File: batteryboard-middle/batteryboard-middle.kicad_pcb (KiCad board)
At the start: 2 copper layers, 46.8 x 46.8 mm, 7 parts, among them J1 Conn 02x10 1.27mm, J2 Conn_01x02, J3 Conn_01x02

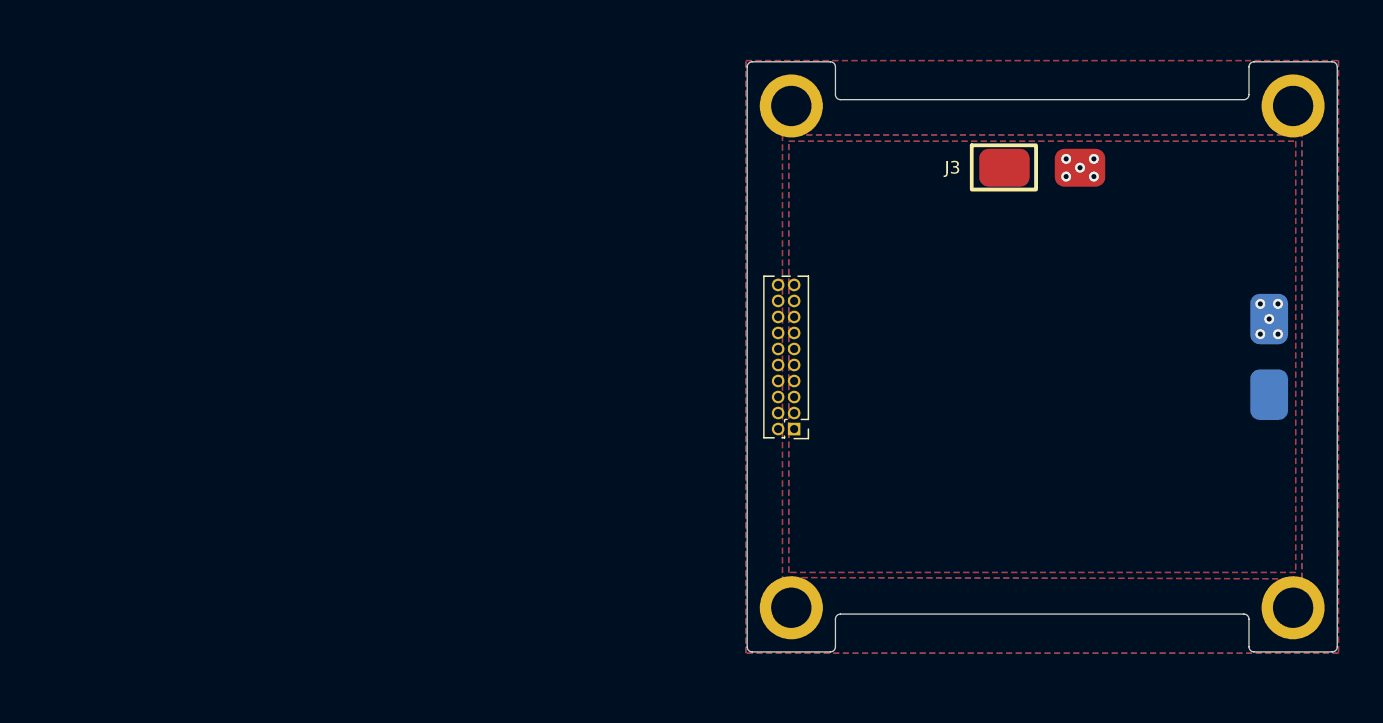
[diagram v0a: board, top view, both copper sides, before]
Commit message: Added proper connectors and added traces
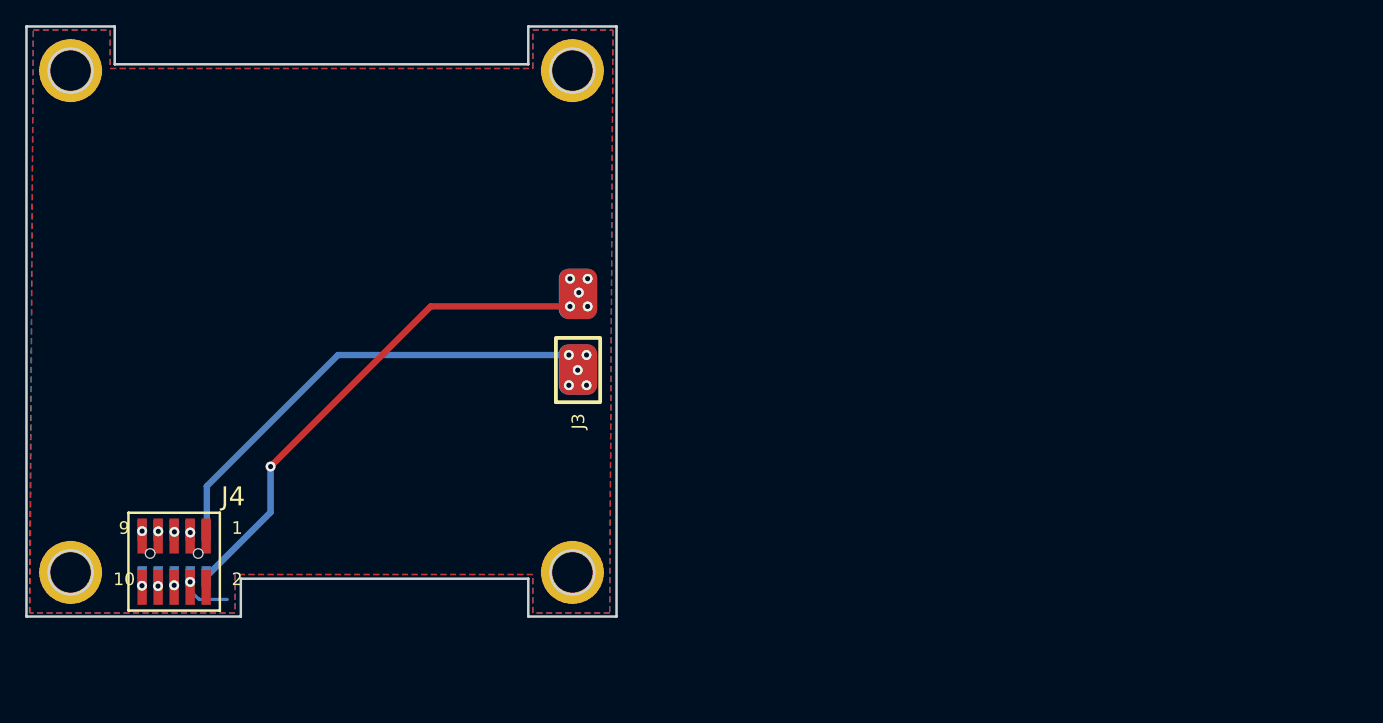
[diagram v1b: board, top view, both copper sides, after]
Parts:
- added J4: Conn_02x05_Odd_Even, batteryboard:SAMTEC-FTS-105-01-X-DV, F.Cu at (76.5, 114.0)
- J1: value Conn 02x10 1.27mm -> Conn_02x05_Odd_Even; footprint Connector_PinHeader_1.27mm:PinHeader_2x10_P1.27mm_Vertical -> batteryboard:SAMTEC_FLE-105-01-G-DV-A; moved to B.Cu
- moved H1 57.2 mm to (68.2, 75.1)
- moved H4 57.2 mm to (68.2, 114.9)
- moved H2 57.2 mm to (108.0, 75.1)
- moved H3 57.2 mm to (108.0, 114.9)
- moved J2 54.9 mm to (108.5, 95.8), turned to 90 degrees
- moved J1 50.2 mm to (76.5, 113.4)
- moved J3 39.0 mm to (108.5, 95.8), turned to 90 degrees
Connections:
- J1 pad 10: unconnected-(J1-Pad10) -> VBUS
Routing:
- net BATT_N_SW: track 0.00 -> 39.9 mm, vias 5 -> 6
- net BATT_P_SW: track 0.00 -> 36.5 mm
- net GND: track 0.00 -> 4.33 mm, vias 0 -> 1
- net VBUS: vias 0 -> 1
- net SDA3: vias 0 -> 1
- net SCL3: vias 0 -> 1
- net COIL_P: vias 0 -> 1
- net COIL_N: vias 0 -> 1
- net BATT_P: vias 0 -> 1
- net +3V3: vias 0 -> 1
- removed copper zone on B.Cu, net BATT_N_SW
- removed copper zone on F.Cu, net BATT_P_SW
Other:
- outline, holes or cut-outs redrawn

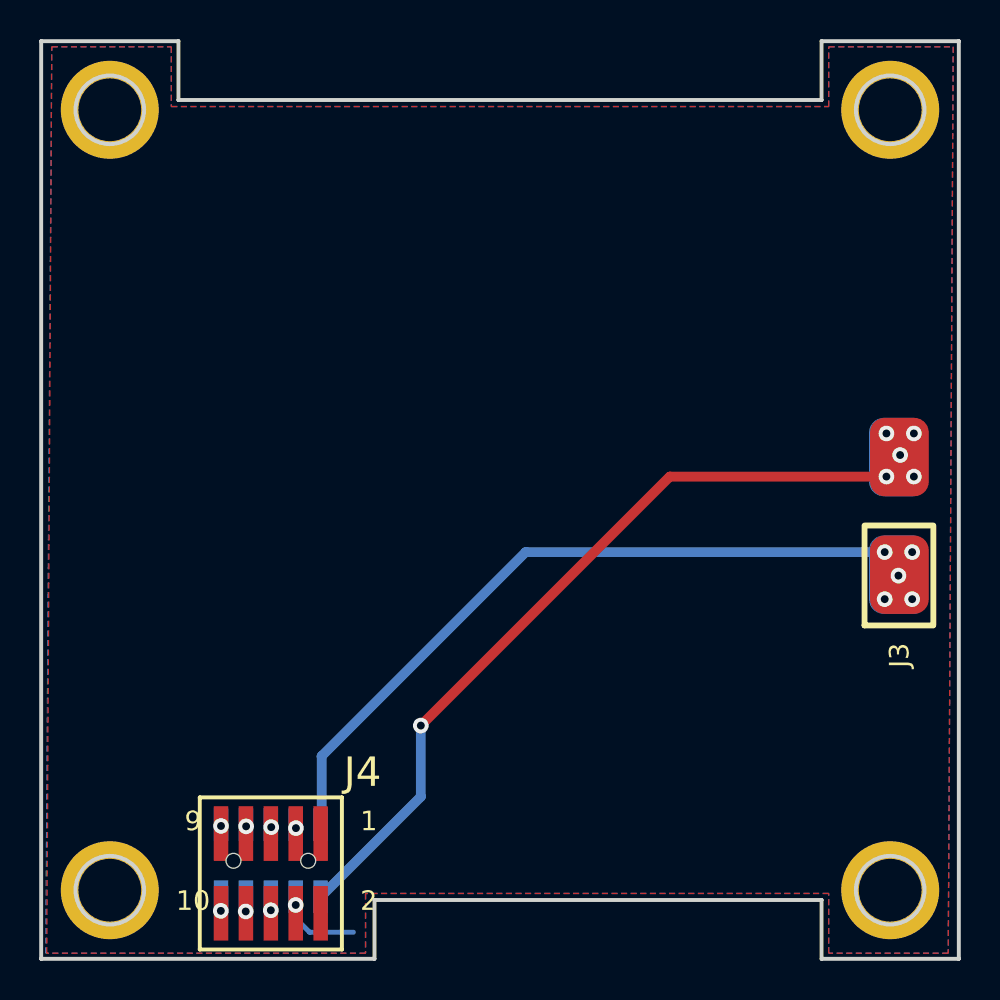
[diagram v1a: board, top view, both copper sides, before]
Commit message: Fixed design errors (some issues remain in middle) and fixed trace widths
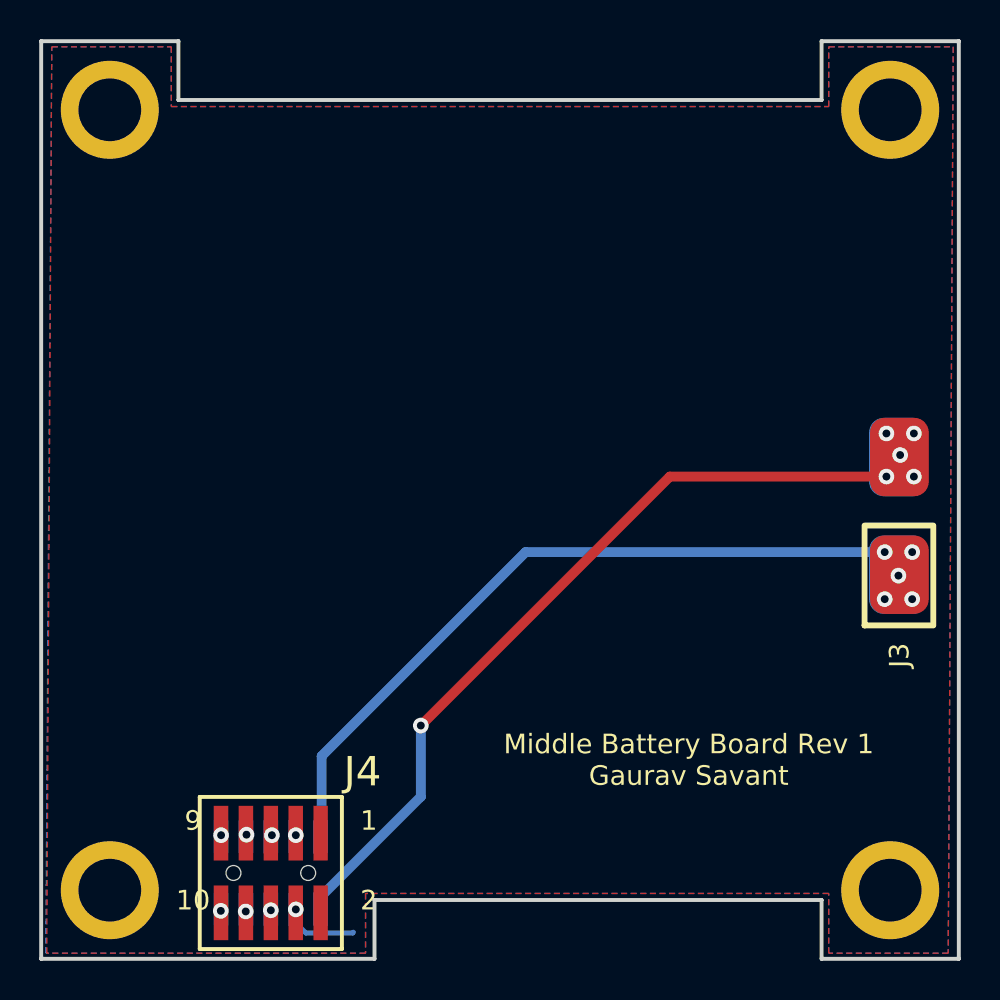
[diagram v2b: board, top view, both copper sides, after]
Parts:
- moved J1 0.62 mm to (76.5, 114.0)
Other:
- outline, holes or cut-outs redrawn
- board text added: "Middle Battery Board Rev 1 Gaurav Savant"
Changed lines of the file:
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@@
   )
   (footprint "batteryboard:SAMTEC-FTS-105-01-X-DV" (layer "F.Cu")
-    (at 76.45 114.042 180)
+    (at 76.45 114.018 180)
     (descr "translated Allegro footprint")
     (property "Sheetfile" "batteryboard-middle.kicad_sch")
@@
   )
   (footprint "batteryboard:SAMTEC_FLE-105-01-G-DV-A" (layer "B.Cu")
-    (at 76.45 113.396 180)
+    (at 76.45 114.018 180)
     (property "Sheetfile" "batteryboard-middle.kicad_sch")
     (property "Sheetname" "")
@@
     (fp_line (start -3.175 1.665) (end 3.175 1.665) (layer "B.Fab") (width 0.1))
     (fp_circle (center -2.85 3.44) (end -2.75 3.44) (layer "B.Fab") (width 0.2) (fill none))
-    (pad "" np_thru_hole circle (at 1.905 0 180) (size 0.76 0.76) (drill 0.76) (layers *.Cu *.Mask))
+    (pad "" np_thru_hole circle (at 1.904988 -0.000009 180) (size 0.76 0.76) (drill 0.76) (layers F&B.Cu *.Mask))
     (pad "" np_thru_hole circle (at -1.905 0 180) (size 0.76 0.76) (drill 0.76) (layers *.Cu *.Mask))
     (pad "01" smd rect (at -2.54 1.8425 180) (size 0.74 1.675) (layers "B.Cu" "B.Paste" "B.Mask")
@@
     )
   )
-  (gr_circle (center 68.238 75.096) (end 69.988 75.096) (layer "Edge.Cuts") (width 0.2) (fill none))
-  (gr_circle (center 108.038 114.896) (end 109.788 114.896) (layer "Edge.Cuts") (width 0.2) (fill none))
-  (gr_circle (center 68.238 114.896) (end 69.988 114.896) (layer "Edge.Cuts") (width 0.2) (fill none))
   (gr_line (start 81.738 115.396) (end 81.738 118.396) (layer "Edge.Cuts") (width 0.2))
   (gr_line (start 104.538 118.396) (end 111.538 118.396) (layer "Edge.Cuts") (width 0.2))
   (gr_line (start 104.538 74.596) (end 71.738 74.596) (layer "Edge.Cuts") (width 0.2))
-  (gr_circle (center 108.038 75.096) (end 109.788 75.096) (layer "Edge.Cuts") (width 0.2) (fill none))
   (gr_line (start 104.538 71.596) (end 104.538 74.596) (layer "Edge.Cuts") (width 0.2))
   (gr_line (start 64.738 71.596) (end 64.738 118.396) (layer "Edge.Cuts") (width 0.2))
@@
   (gr_line (start 111.538 71.596) (end 104.538 71.596) (layer "Edge.Cuts") (width 0.2))
   (gr_line (start 111.538 71.596) (end 111.538 118.396) (layer "Edge.Cuts") (width 0.2))
+  (gr_text "Middle Battery Board Rev 1\nGaurav Savant\n" (at 97.7646 108.2548) (layer "F.SilkS")
+    (effects (font (size 1 1) (thickness 0.15)))
+  )
   (via (at 109.158 97.6532) (size 0.8) (drill 0.4) (layers "F.Cu" "B.Cu") (net 1))
   (via (at 107.758 100.0532) (size 0.8) (drill 0.4) (layers "F.Cu" "B.Cu") (net 1))
@@
   (segment (start 78.99 115.2385) (end 84.1 110.1285) (width 0.5) (layer "B.Cu") (net 2))
   (segment (start 84.1 110.1285) (end 84.1 106.5) (width 0.5) (layer "B.Cu") (net 2))
-  (via (at 77.72 115.65) (size 0.8) (drill 0.4) (layers "F.Cu" "B.Cu") (net 3))
-  (segment (start 78.43 117.04) (end 80.66 117.04) (width 0.254) (layer "B.Cu") (net 3))
-  (segment (start 77.72 115.2385) (end 77.72 115.65) (width 0.254) (layer "B.Cu") (net 3))
-  (segment (start 77.72 115.65) (end 77.72 116.33) (width 0.254) (layer "B.Cu") (net 3))
-  (segment (start 77.72 116.33) (end 78.43 117.04) (width 0.254) (layer "B.Cu") (net 3))
-  (via (at 77.73 111.73) (size 0.8) (drill 0.4) (layers "F.Cu" "B.Cu") (net 4))
-  (via (at 76.47 111.68) (size 0.8) (drill 0.4) (layers "F.Cu" "B.Cu") (net 5))
+  (via (at 77.724 115.8748) (size 0.8) (drill 0.4) (layers "F.Cu" "B.Cu") (net 3))
+  (segment (start 77.724 116.563022) (end 78.239489 117.078511) (width 0.254) (layer "B.Cu") (net 3))
+  (segment (start 80.621489 117.078511) (end 80.66 117.04) (width 0.254) (layer "B.Cu") (net 3))
+  (segment (start 77.72 115.2385) (end 77.72 115.8708) (width 0.254) (layer "B.Cu") (net 3))
+  (segment (start 77.724 115.8748) (end 77.724 116.563022) (width 0.254) (layer "B.Cu") (net 3))
+  (segment (start 77.72 115.8708) (end 77.724 115.8748) (width 0.254) (layer "B.Cu") (net 3))
+  (segment (start 78.239489 117.078511) (end 80.621489 117.078511) (width 0.254) (layer "B.Cu") (net 3))
+  (via (at 77.724 112.0902) (size 0.8) (drill 0.4) (layers "F.Cu" "B.Cu") (net 4))
+  (via (at 76.5048 112.0902) (size 0.8) (drill 0.4) (layers "F.Cu" "B.Cu") (net 5))
   (via (at 76.45 115.92) (size 0.8) (drill 0.4) (layers "F.Cu" "B.Cu") (net 6))
-  (via (at 75.19 111.64) (size 0.8) (drill 0.4) (layers "F.Cu" "B.Cu") (net 7))
+  (via (at 75.2094 112.0648) (size 0.8) (drill 0.4) (layers "F.Cu" "B.Cu") (net 7))
   (via (at 75.17 115.98) (size 0.8) (drill 0.4) (layers "F.Cu" "B.Cu") (net 8))
-  (via (at 73.91 111.62) (size 0.8) (drill 0.4) (layers "F.Cu" "B.Cu") (net 9))
+  (via (at 73.914 112.0902) (size 0.8) (drill 0.4) (layers "F.Cu" "B.Cu") (net 9))
   (via (at 73.9 115.95) (size 0.8) (drill 0.4) (layers "F.Cu" "B.Cu") (net 10))
   (zone (net 3) (net_name "GND") (layer "F.Cu") (hatch edge 0.508)
@@
   (group "" (id 199946a1-d931-4a51-b109-669174053557)
     (members
-      01a5bbd7-c875-416a-8bd8-1617e0702a52
-      03420a08-e50a-4a71-8807-dc69691d52e9
-      13b43084-4a18-4b09-9d99-27dcc0f95f55
       35f23d10-1aa0-4ca4-9a63-c264cbbfe9ad
       45fe3717-b1bb-4dba-aa83-ecfb1f152bc7
       479f44c2-6827-49e1-beac-048720d4d6e8
-      55272316-5c3c-4de3-bbd8-c6dbf76c30ac
       555b1bf8-086b-434a-b0cf-629ff9785013
       6cfea132-fcb5-4a65-8bba-2b3aa13c6f00

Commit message: Fixes and cleanup
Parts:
- added Ref**: Val**, custom-footprints:pycubed_mini_half, F.Cu at (147.6, 80.2)
- J4: footprint batteryboard:SAMTEC-FTS-105-01-X-DV -> batteryboard:FTS-105-XX-YY-DV-A
- moved H1 98.6 mm to (166.7, 80.7), turned to -90 degrees
- moved H2 74.2 mm to (166.7, 120.5), turned to -90 degrees
- moved H4 67.9 mm to (126.9, 80.7), turned to -90 degrees
- moved J1 57.1 mm to (127.8, 89.0), turned to 90 degrees
- moved J4 57.1 mm to (127.8, 89.0), turned to 90 degrees
- moved J2 45.2 mm to (146.0, 120.9), turned to 180 degrees
- moved J3 45.1 mm to (146.0, 121.0), turned to 180 degrees
- moved H3 19.7 mm to (126.9, 120.5), turned to -90 degrees
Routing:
- net GND: track 4.49 -> 0.00 mm
- net BATT_N_SW: track 39.9 -> 36.5 mm, vias 6 -> 5
- net BATT_P_SW: track 36.5 -> 37.4 mm
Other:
- outline, holes or cut-outs redrawn
- board text added: "09-JUN-22"
- board text added: "v01"

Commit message: add + and - symbols
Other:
- board text added: "+"
- board text added: "-"
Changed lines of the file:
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@@
   (gr_line (start 170.200008 123.599997) (end 170.200008 117.400009) (layer "Edge.Cuts") (width 0.0254))
   (gr_line (start 169.800009 123.999996) (end 123.799999 123.999996) (layer "Edge.Cuts") (width 0.0254))
+  (gr_text "+" (at 154.4 120.5) (layer "B.SilkS")
+    (effects (font (size 4 4) (thickness 0.7)) (justify mirror))
+  )
+  (gr_text "-" (at 137.8 120.6) (layer "B.SilkS")
+    (effects (font (size 4 4) (thickness 0.7)) (justify mirror))
+  )
+  (gr_text "+" (at 154.4 120.5) (layer "F.SilkS")
+    (effects (font (size 4 4) (thickness 0.7)) (justify mirror))
+  )
   (gr_text "Middle Battery Board Rev 1\nGaurav Savant\n" (at 129.3 104.8 90) (layer "F.SilkS")
     (effects (font (size 1 1) (thickness 0.15)))
   )
+  (gr_text "-" (at 137.8 120.6) (layer "F.SilkS")
+    (effects (font (size 4 4) (thickness 0.7)) (justify mirror))
+  )
   (gr_text "09-JUN-22" (at 148.7 79.9) (layer "F.Mask")
